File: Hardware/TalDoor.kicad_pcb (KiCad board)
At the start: 2 copper layers, 118.2 x 60.3 mm, 67 parts, among them J1 SI-52003-F_RJ45, J2 Screw_Terminal_01x02, J3 Conn_01x06_Male, J4 Conn_01x06_Male, M2 Screw MountingHole_2.2mm_M2_Pad_Via, P1 PocketBeagle, Q1 RK7002BM, Q2 BSS223PWH6327XTSA1, U1 DRV8837, U2 ENC28J60-I/SO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

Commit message: Started changed base on Hardware 1 build
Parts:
- removed C18, C19: 1uF, Capacitors_SMD:C_0603
- C17: value 1uF -> 10uF; footprint Capacitors_SMD:C_0603 -> Capacitors_SMD:C_0805
- J2: value Screw_Terminal_01x02 -> Conn_01x02
- U1: footprint Housings_SON:WSON-8_1EP_2x2mm_Pitch0.5mm_ThermalVias -> TalDoor_Footprints:WSON-8_1EP_2x2mm_Pitch0.5mm_ThermalVias
- U5: value CAT3200-5 -> NCP1117-3.3_SOT223; footprint TO_SOT_Packages_SMD:SOT-23-6 -> TO_SOT_Packages_SMD:SOT-223-3_TabPin2
- moved C17 65.9 mm to (112.7, 181.6)
- moved C14 44.3 mm to (156.2, 106.1), turned to 180 degrees
- moved C11 44.1 mm to (172.2, 106.4), turned to 180 degrees
- moved U5 42.6 mm to (126.1, 158.2)
- moved R5 41.1 mm to (155.4, 108.1), turned to 270 degrees
- moved R6 39.9 mm to (157.0, 108.2), turned to 270 degrees
- moved R7 39.0 mm to (158.5, 108.2), turned to 270 degrees
- moved R2 38.0 mm to (160.6, 108.2), turned to 270 degrees
- moved R1 37.6 mm to (162.2, 108.1), turned to 270 degrees
- moved J1 28.8 mm to (169.5, 147.0)
- moved U2 22.6 mm to (163.9, 115.5), turned to 270 degrees
- moved C2 18.3 mm to (155.7, 123.0), turned to 270 degrees
- moved C6 18.1 mm to (172.2, 123.0), turned to 270 degrees
- moved R9 15.3 mm to (157.3, 123.1), turned to 90 degrees
- moved L1 15.2 mm to (156.6, 128.6), turned to 180 degrees
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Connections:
- C1 pad 2: Net-(C1-Pad2) -> +5V
- C12 pad 1: +3V3 -> +5V
- C13 pad 1: +3V3 -> +5V
- C15 pad 1: +3V3 -> +5V
- C17 pad 1: GND -> +3V3
- C17 pad 2: +3V3 -> GND
- C8 pad 2: +3V3 -> +5V
- J3 pad 1: +3V3 -> /SCL
- J3 pad 2: GND -> /SDA
- J3 pad 3: /PRU0_0 -> /PRU1_10
- J3 pad 4: /PRU1_10 -> /PRU0_0
- J3 pad 5: /SDA -> GND
- J3 pad 6: /SCL -> +3V3
- P1 pad 1.1: Net-(P1-Pad1.1) -> +5V
- P1 pad 1.16: GND -> Net-(P1-Pad1.16)
- P1 pad 1.18: +3V3 -> Net-(P1-Pad1.18)
- P1 pad 1.22: GND -> Net-(P1-Pad1.22)
- P1 pad 2.14: +3V3 -> Net-(P1-Pad2.14)
- P1 pad 2.15: GND -> Net-(P1-Pad2.15)
- P1 pad 2.21: GND -> Net-(P1-Pad2.21)
- Q2 pad 2: Net-(D5-Pad2) -> /+3.3v2
- Q2 pad 3: /+3.3v2 -> Net-(D5-Pad2)
- U1 pad 1: Net-(C1-Pad2) -> +5V
- U1 pad 7: +3V3 -> +5V
- U1 pad 8: +3V3 -> +5V
- U4 pad 8: +3V3 -> +5V
- U5 pad 1: Net-(C1-Pad2) -> GND
- U5 pad 2: GND -> +3V3
- U5 pad 3: +3V3 -> +5V
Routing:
- net +5V: track 0.00 -> 170.2 mm, vias 0 -> 35
- net +3V3: track 174.3 -> 7.12 mm, vias 37 -> 2
- net /PRU1_10: track 68.1 -> 9.08 mm
- net /PRU0_0: track 62.7 -> 8.45 mm
- net /SCL: track 69.5 -> 42.7 mm
- net /SDA: track 71.5 -> 47.3 mm
- net Net-(J1-PadG-): track 23.7 -> 0.03 mm, vias 1 -> 0
- net Net-(J1-Pad4): track 53.5 -> 32.0 mm
- net Net-(J1-Pad9): track 21.0 -> 0.00 mm
- net Net-(C16-Pad1): track 29.9 -> 9.08 mm
- net /LEDA: track 25.3 -> 4.95 mm
- net Net-(J1-Pad5): track 50.0 -> 30.5 mm
- net Net-(J1-Pad8): track 19.0 -> 0.00 mm
- net Net-(J1-Pad1): track 39.0 -> 20.8 mm
- net Net-(J1-Pad10): track 18.2 -> 0.00 mm
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
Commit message: Updating PCB layout, unfinished
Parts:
- moved P1 48.3 mm to (104.9, 152.3), turned to 180 degrees
- moved C17 28.8 mm to (131.1, 159.4), turned to 270 degrees
- moved R4 18.2 mm to (155.6, 130.9), turned to 180 degrees
- moved R3 18.0 mm to (158.2, 130.9), turned to 0 degrees
- moved U1 11.2 mm to (138.8, 111.1)
- moved C8 11.2 mm to (136.9, 113.1)
- moved C1 11.2 mm to (140.4, 113.1)
- moved G*** 10.6 mm to (99.9, 167.0)
- moved J2 1.66 mm to (137.8, 106.9)
- moved J1 1.02 mm to (168.5, 147.1)
- moved R2 1.02 mm to (159.6, 108.2)
- moved U2 1.02 mm to (162.9, 115.5)
- moved Y1 1.02 mm to (167.9, 127.3)
- moved C11 1.02 mm to (171.2, 106.4)
- moved C14 1.02 mm to (155.2, 106.1)
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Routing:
- net +5V: track 170.2 -> 268.1 mm, vias 35 -> 33
- net /PRU0_0: track 8.45 -> 66.2 mm
- net /PRU1_10: track 9.08 -> 59.6 mm
- net Net-(J1-Pad9): track 0.00 -> 46.6 mm
- net /LEDA: track 4.95 -> 50.8 mm
- net Net-(J1-Pad8): track 0.00 -> 45.7 mm
- net Net-(J1-Pad10): track 0.00 -> 42.6 mm
- net +3V3: track 7.12 -> 46.0 mm, vias 2 -> 4
- net /PRU0_1: track 47.1 -> 8.43 mm, vias 1 -> 0
- net Net-(J1-Pad11): track 0.00 -> 37.7 mm
- net /PRU0_4: track 45.4 -> 9.70 mm, vias 1 -> 0
- net /LEDB: track 4.97 -> 40.0 mm
- net Net-(J1-Pad4): track 32.0 -> 52.6 mm, vias 2 -> 0
- net Net-(J1-Pad5): track 30.5 -> 50.1 mm
- net GND: track 205.6 -> 224.2 mm, vias 44 -> 45
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- added copper zone on B.Cu, net +5V
- added copper zone on F.Cu, net +5V
- removed copper zone on B.Cu, net +3V3
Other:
- board size 118.2 x 60.3 mm -> 117.2 x 60.3 mm
- board text added: "<"
- board text added: "["

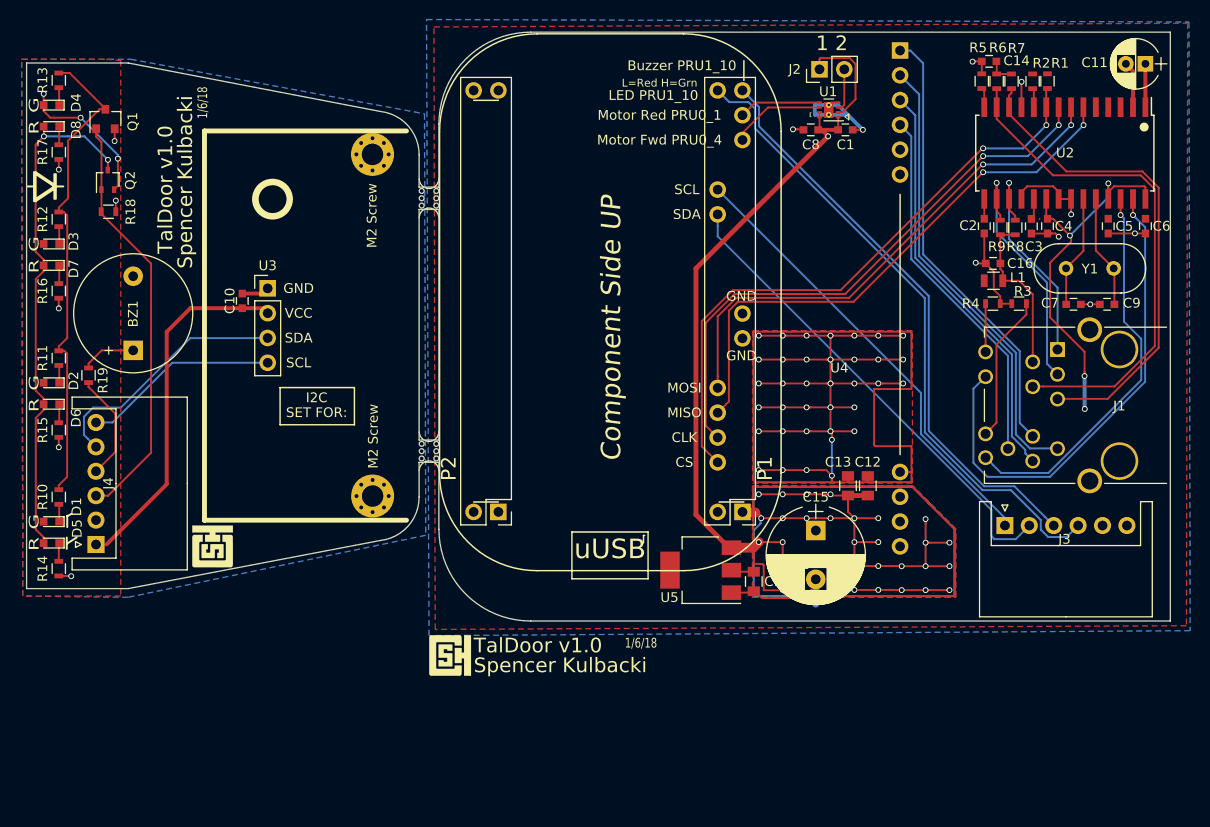
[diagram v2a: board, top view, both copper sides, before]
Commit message: fixed fills so there is no DRC error
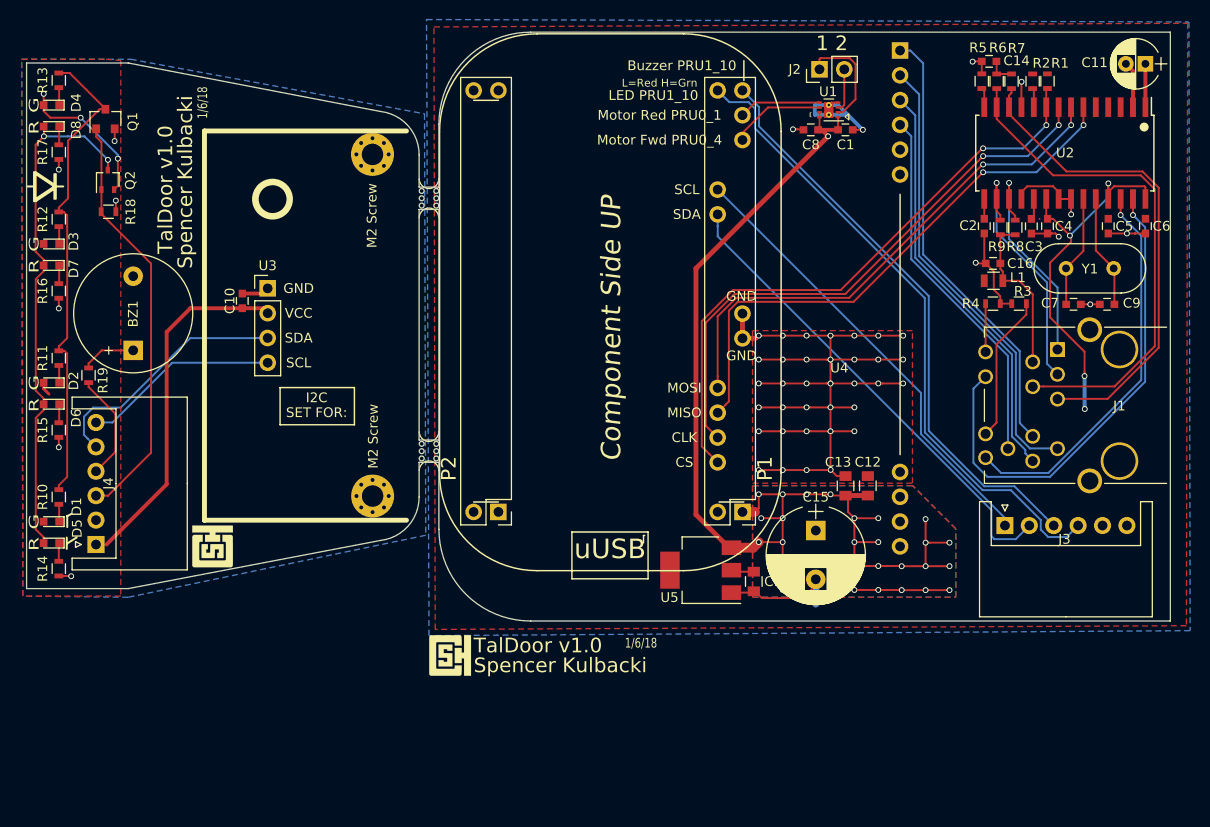
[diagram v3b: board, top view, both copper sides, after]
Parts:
- moved C13 0.25 mm to (140.5, 149.6)
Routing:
- net +5V: track 268.1 -> 144.3 mm, vias 33 -> 29
- net GND: track 224.2 -> 154.2 mm, vias 45 -> 44
- net /+3.3v2: track 52.0 -> 53.4 mm

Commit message: Updated PCB layout for fixes from v1
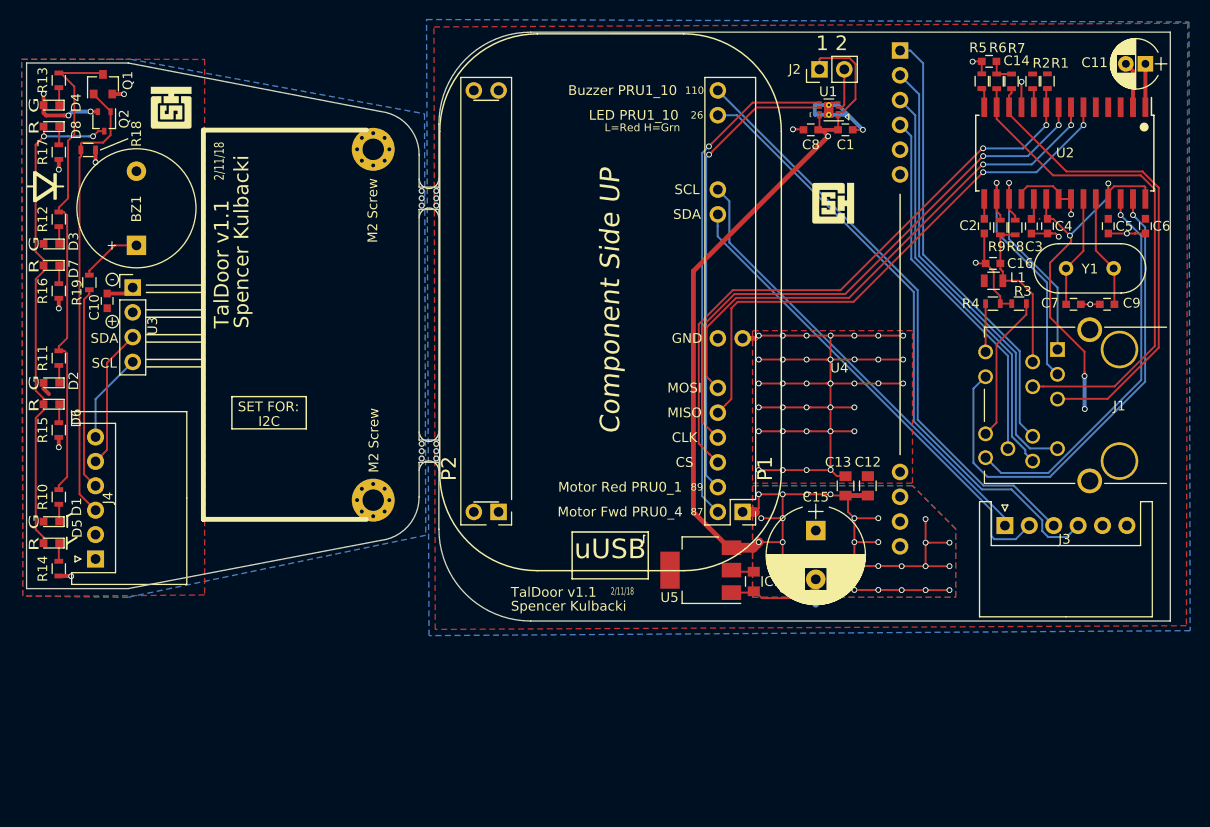
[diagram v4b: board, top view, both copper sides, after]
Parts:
- C15: value 1000uF -> 470uF
- moved G*** 60.7 mm to (139.2, 120.7)
- moved G*** 45.1 mm to (71.4, 110.9)
- moved C10 13.8 mm to (64.8, 130.7)
- moved U3 13.8 mm to (67.4, 129.3)
- moved BZ1 10.8 mm to (67.8, 125.0)
- moved R19 9.51 mm to (63.0, 128.8)
- moved R18 6.66 mm to (62.9, 115.2)
- moved Q2 6.00 mm to (64.5, 112.3), turned to 270 degrees
- moved Q1 3.57 mm to (64.4, 108.5)
- moved J4 1.49 mm to (63.6, 157.1)
- moved M2 Screw 0.53 mm to (92.1, 115.1)
- moved M2 Screw 0.42 mm to (92.1, 151.1)
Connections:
- P1 pad 1.2: Net-(P1-Pad1.2) -> /PRU0_1
- P1 pad 1.36: /PRU0_0 -> /PRU1_10
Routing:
- net /+3.3v2: track 53.4 -> 9.24 mm
- net /PRU0_1: track 8.43 -> 51.6 mm, vias 0 -> 1
- net /PRU0_4: track 9.70 -> 48.0 mm, vias 0 -> 1
- net Net-(J4-Pad5): track 25.8 -> 14.3 mm
- net Net-(J4-Pad6): track 20.1 -> 9.47 mm
- net Net-(J4-Pad4): track 11.0 -> 21.2 mm
- net Net-(J4-Pad3): track 43.0 -> 46.6 mm
- net GND: track 154.2 -> 151.6 mm
- net /PRU0_0: track 66.2 -> 63.7 mm
- net Net-(D5-Pad2): track 53.3 -> 51.1 mm
- net Net-(Q1-Pad3): track 49.7 -> 50.8 mm
- net /PRU1_10: track 59.6 -> 60.6 mm
- net /MOSI: track 53.5 -> 54.4 mm
- net Net-(BZ1-Pad1): track 5.58 -> 6.35 mm
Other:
- board text added: "2/11/18"
- board text added: "TalDoor v1.1"
- board text removed: "1/6/18"
- board text removed: "TalDoor v1.0"

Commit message: Updated PCB with solder jumpers for easier developing
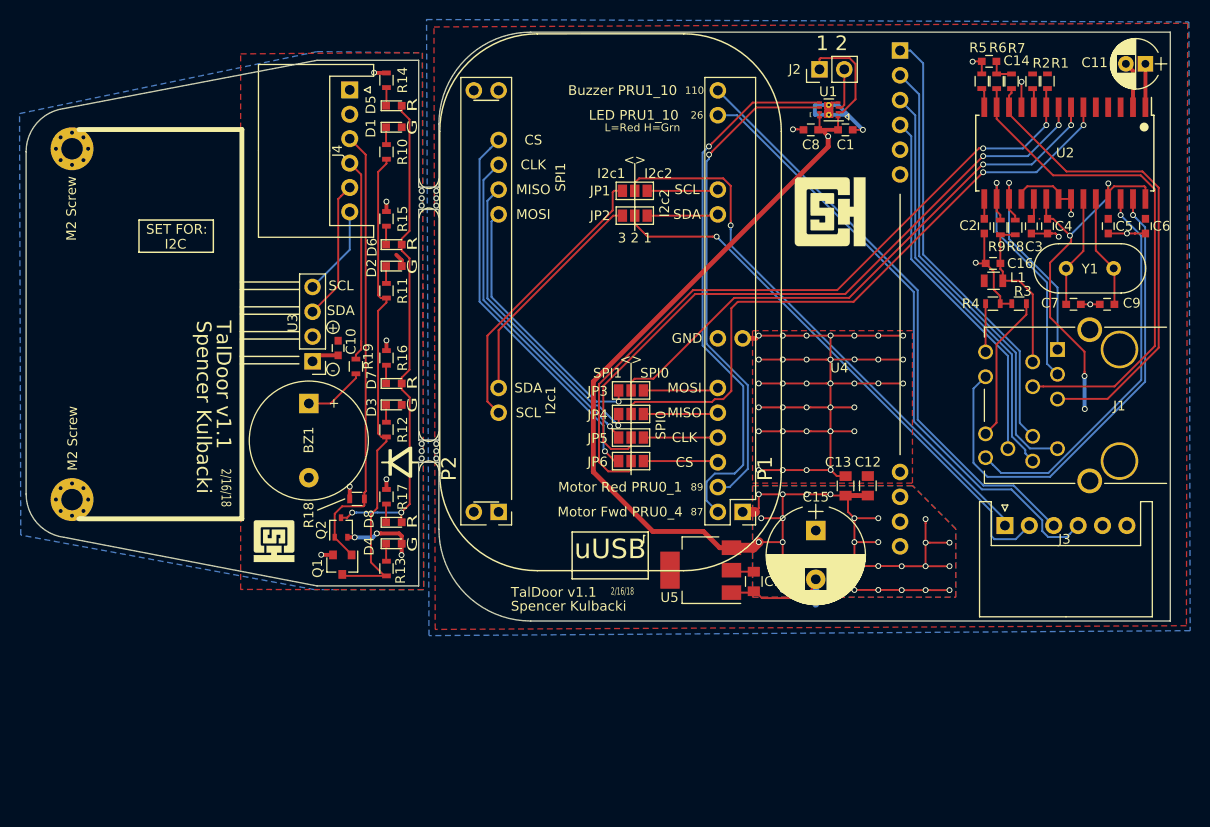
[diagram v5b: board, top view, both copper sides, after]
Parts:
- removed the G*** at (139.2, 120.7)
- added G***: LOGO, TalDoor_Footprints:CSH_logo_Fsilk_bigger, F.Cu at (138.9, 121.5)
- added G***: LOGO, TalDoor_Footprints:CSH_logo_Fsilk_bigger, B.Cu at (169.2, 159.0)
- added JP1: Jumper_NC_Dual, Connectors:GS3, F.Cu at (118.9, 119.4)
- added JP2: Jumper_NC_Dual, Connectors:GS3, F.Cu at (118.9, 121.9)
- added JP3: Jumper_NC_Dual, Connectors:GS3, F.Cu at (118.5, 139.8)
- added JP4: Jumper_NC_Dual, Connectors:GS3, F.Cu at (118.5, 142.2)
- added JP5: Jumper_NC_Dual, Connectors:GS3, F.Cu at (118.5, 144.7)
- added JP6: Jumper_NC_Dual, Connectors:GS3, F.Cu at (118.5, 147.1)
- P1: footprint TalDoor_Footprints:PocketBeagle_TalDoor -> TalDoor_Footprints:PocketBeagle_DEV_TalDoor
- moved R14 60.3 mm to (93.4, 108.0), turned to 90 degrees
- moved R13 60.2 mm to (93.4, 158.1), turned to 270 degrees
- moved D4 57.0 mm to (94.2, 155.5), turned to 0 degrees
- moved D5 56.9 mm to (94.2, 110.7), turned to 0 degrees
- moved Q1 55.0 mm to (88.9, 157.7), turned to 270 degrees
- moved J4 54.7 mm to (89.7, 109.0), turned to 270 degrees
- moved D8 53.6 mm to (94.2, 153.3), turned to 0 degrees
- moved D1 53.5 mm to (94.2, 112.9), turned to 0 degrees
- moved R10 48.7 mm to (93.4, 115.4), turned to 270 degrees
- moved R17 48.7 mm to (93.4, 150.7), turned to 90 degrees
- moved Q2 48.2 mm to (88.8, 153.9), turned to 90 degrees
- moved M2 Screw 47.4 mm to (61.2, 115.1), turned to 270 degrees
- moved M2 Screw 47.3 mm to (61.2, 151.0), turned to 270 degrees
- moved G*** 45.6 mm to (81.9, 155.3), turned to 270 degrees
- moved R18 45.1 mm to (90.4, 150.9), turned to 0 degrees
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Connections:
- P1 pad 1.10: /MISO -> /MISO1
- P1 pad 1.12: /MOSI -> /MOSI1
- P1 pad 1.26: /SDA -> /SDA2
- P1 pad 1.28: /SCL -> /SCL2
- P1 pad 1.6: /CS -> /CS1
- P1 pad 1.8: /CLK -> /CLK1
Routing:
- net /CS2: track 0.00 -> 39.8 mm, vias 0 -> 1
- net /CLK2: track 0.00 -> 34.3 mm, vias 0 -> 1
- net /MISO2: track 0.00 -> 31.6 mm, vias 0 -> 1
- net /SCL1: track 0.00 -> 29.4 mm
- net /MOSI2: track 0.00 -> 27.4 mm, vias 0 -> 1
- net /SDA1: track 0.00 -> 23.5 mm
- net +5V: track 144.5 -> 156.6 mm
- net /SCL: track 46.6 -> 57.6 mm, vias 0 -> 1
- net /CLK: track 58.9 -> 69.4 mm
- net /CS: track 62.8 -> 73.2 mm
- net /MISO: track 57.0 -> 65.9 mm
- net /MOSI1: track 0.00 -> 7.73 mm
- net /MISO1: track 0.00 -> 7.67 mm
- net /CS1: track 0.00 -> 7.67 mm
- net /CLK1: track 0.00 -> 7.62 mm
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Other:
- outline, holes or cut-outs redrawn
- board text added: "2/16/18"
- board text added: "3 2 1"
- board text added: "<>"
- board text added: "I2c1"
- board text added: "I2c2"
- board text added: "It's all about Tal"
- board text added: "SPI0"
- board text added: "SPI1"
- board text removed: "2/11/18"
